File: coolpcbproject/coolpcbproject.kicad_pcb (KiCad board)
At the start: 2 copper layers, 106.7 x 38.1 mm, 24 parts, among them SW1 SW_Push, U1 ATmega32U4-A, Y1 16 MHz

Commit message: finished initial draft
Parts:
- added R5: 5.1K, Resistor_SMD:R_0805_2012Metric, B.Cu at (135.4, 89.0)
- added R6: 5.1K, Resistor_SMD:R_0805_2012Metric, B.Cu at (140.7, 89.0)
- added U2: USBLC6-2SC6, Package_TO_SOT_SMD:SOT-23-6, B.Cu at (137.9, 96.3)
- C1, C2, C3, C4, C5, C6, C7, D1, D2, D3, D4, F1, R1, R2, R3, R4, SW1, U1, Y1: moved to B.Cu
- USB1: value Molex-0548190589 -> HRO-TYPE-C-31-M-12; moved to B.Cu
- moved C1 44.0 mm to (169.7, 85.9), turned to -90 degrees
- moved C2 34.3 mm to (161.0, 85.9), turned to 90 degrees
- moved R4 32.2 mm to (173.6, 102.4), turned to -90 degrees
- moved R3 31.5 mm to (151.1, 101.9), turned to -90 degrees
- moved Y1 28.2 mm to (165.4, 85.9)
- moved R2 24.5 mm to (151.2, 98.2)
- moved F1 23.1 mm to (137.9, 91.8), turned to 180 degrees
- moved C3 19.7 mm to (156.0, 96.4), turned to -90 degrees
- moved SW1 17.6 mm to (140.8, 107.1)
- moved USB1 16.0 mm to (137.9, 77.8), turned to 0 degrees
- moved C5 13.9 mm to (173.6, 93.9), turned to -90 degrees
- moved C6 13.2 mm to (168.0, 105.4)
- moved C7 11.7 mm to (156.0, 101.3), turned to 90 degrees
- moved R1 11.6 mm to (151.4, 87.1), turned to -90 degrees
- moved U1 7.00 mm to (164.6, 97.0)
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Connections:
- C1 pad 1: (no net) -> GND
- C1 pad 2: (no net) -> Net-(C1-Pad2)
- C2 pad 1: (no net) -> GND
- C2 pad 2: (no net) -> Net-(C2-Pad2)
- C3 pad 1: (no net) -> Net-(C3-Pad1)
- C3 pad 2: (no net) -> GND
- C4 pad 1: (no net) -> GND
- C4 pad 2: (no net) -> +5V
- C5 pad 1: (no net) -> GND
- C5 pad 2: (no net) -> +5V
- C6 pad 1: (no net) -> GND
- C6 pad 2: (no net) -> +5V
- C7 pad 1: (no net) -> GND
- C7 pad 2: (no net) -> +5V
- D1 pad 1: (no net) -> row0
- D1 pad 2: (no net) -> Net-(D1-Pad2)
- D2 pad 1: (no net) -> row0
- D2 pad 2: (no net) -> Net-(D2-Pad2)
- D3 pad 1: (no net) -> row1
- D3 pad 2: (no net) -> Net-(D3-Pad2)
- D4 pad 1: (no net) -> row1
- D4 pad 2: (no net) -> Net-(D4-Pad2)
- F1 pad 1: (no net) -> Net-(F1-Pad1)
- F1 pad 2: (no net) -> +5V
- MX1 pad 1: (no net) -> col0
- MX1 pad 2: (no net) -> Net-(D1-Pad2)
- MX2 pad 1: (no net) -> col1
- MX2 pad 2: (no net) -> Net-(D2-Pad2)
- MX3 pad 1: (no net) -> col0
- MX3 pad 2: (no net) -> Net-(D3-Pad2)
- MX4 pad 1: (no net) -> col1
- MX4 pad 2: (no net) -> Net-(D4-Pad2)
- R1 pad 1: (no net) -> Net-(R1-Pad1)
- R1 pad 2: (no net) -> GND
- R2 pad 1: (no net) -> D+
- R2 pad 2: (no net) -> Net-(R2-Pad2)
- R3 pad 1: (no net) -> D-
- R3 pad 2: (no net) -> Net-(R3-Pad2)
- R4 pad 1: (no net) -> Net-(R4-Pad1)
- R4 pad 2: (no net) -> GND
- SW1 pad 1: (no net) -> GND
- SW1 pad 2: (no net) -> Net-(R1-Pad1)
- U1 pad 1: (no net) -> unconnected-(U1-Pad1)
- U1 pad 10: (no net) -> unconnected-(U1-Pad10)
- U1 pad 11: (no net) -> unconnected-(U1-Pad11)
- U1 pad 12: (no net) -> unconnected-(U1-Pad12)
- U1 pad 13: (no net) -> Net-(R1-Pad1)
- U1 pad 14: (no net) -> +5V
- U1 pad 15: (no net) -> GND
- U1 pad 16: (no net) -> Net-(C2-Pad2)
- U1 pad 17: (no net) -> Net-(C1-Pad2)
- U1 pad 18: (no net) -> unconnected-(U1-Pad18)
- U1 pad 19: (no net) -> unconnected-(U1-Pad19)
- U1 pad 2: (no net) -> +5V
- U1 pad 20: (no net) -> unconnected-(U1-Pad20)
- U1 pad 21: (no net) -> unconnected-(U1-Pad21)
- U1 pad 22: (no net) -> unconnected-(U1-Pad22)
- U1 pad 23: (no net) -> GND
- U1 pad 24: (no net) -> +5V
- U1 pad 25: (no net) -> unconnected-(U1-Pad25)
- U1 pad 26: (no net) -> unconnected-(U1-Pad26)
- U1 pad 27: (no net) -> row0
- U1 pad 28: (no net) -> col1
- U1 pad 29: (no net) -> col0
- U1 pad 3: (no net) -> Net-(R3-Pad2)
- U1 pad 30: (no net) -> row1
- U1 pad 31: (no net) -> unconnected-(U1-Pad31)
- U1 pad 32: (no net) -> unconnected-(U1-Pad32)
- U1 pad 33: (no net) -> Net-(R4-Pad1)
- U1 pad 34: (no net) -> +5V
- U1 pad 35: (no net) -> GND
- U1 pad 36: (no net) -> unconnected-(U1-Pad36)
- U1 pad 37: (no net) -> unconnected-(U1-Pad37)
- U1 pad 38: (no net) -> unconnected-(U1-Pad38)
- U1 pad 39: (no net) -> unconnected-(U1-Pad39)
- U1 pad 4: (no net) -> Net-(R2-Pad2)
- U1 pad 40: (no net) -> unconnected-(U1-Pad40)
- U1 pad 41: (no net) -> unconnected-(U1-Pad41)
- U1 pad 42: (no net) -> unconnected-(U1-Pad42)
- U1 pad 43: (no net) -> GND
- U1 pad 44: (no net) -> +5V
- U1 pad 5: (no net) -> GND
- U1 pad 6: (no net) -> Net-(C3-Pad1)
- U1 pad 7: (no net) -> +5V
- U1 pad 8: (no net) -> unconnected-(U1-Pad8)
- U1 pad 9: (no net) -> unconnected-(U1-Pad9)
- USB1 pad 1: (no net) -> GND
- USB1 pad 10: (no net) -> Net-(R6-Pad2)
- USB1 pad 11: (no net) -> Net-(F1-Pad1)
- USB1 pad 12: (no net) -> GND
- USB1 pad 13: (no net) -> GND
- USB1 pad 2: (no net) -> Net-(F1-Pad1)
- USB1 pad 3: (no net) -> unconnected-(USB1-Pad3)
- USB1 pad 4: (no net) -> Net-(R5-Pad2)
- USB1 pad 5: (no net) -> D- IN
- USB1 pad 6: (no net) -> D+ IN
- USB1 pad 7: (no net) -> D- IN
- USB1 pad 8: (no net) -> D+ IN
- USB1 pad 9: (no net) -> unconnected-(USB1-Pad9)
- Y1 pad 1: (no net) -> Net-(C2-Pad2)
- Y1 pad 2: (no net) -> GND
- Y1 pad 3: (no net) -> Net-(C1-Pad2)
- Y1 pad 4: (no net) -> GND
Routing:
- net GND: track 0.00 -> 138.4 mm
- net +5V: track 0.00 -> 75.8 mm, vias 0 -> 2
- net row1: track 0.00 -> 58.8 mm
- net col1: track 0.00 -> 56.5 mm
- net row0: track 0.00 -> 48.5 mm
- net col0: track 0.00 -> 37.2 mm
- net Net-(R1-Pad1): track 0.00 -> 36.3 mm, vias 0 -> 2
- net Net-(R3-Pad2): track 0.00 -> 17.2 mm
- net D- IN: track 0.00 -> 13.5 mm
- net Net-(R2-Pad2): track 0.00 -> 13.0 mm
- net D+ IN: track 0.00 -> 11.8 mm
- net Net-(C2-Pad2): track 0.00 -> 11.0 mm
- net Net-(D1-Pad2): track 0.00 -> 8.54 mm
- net Net-(C1-Pad2): track 0.00 -> 8.52 mm
- net Net-(D4-Pad2): track 0.00 -> 8.50 mm
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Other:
- board size 106.7 x 38.1 mm -> 90.9 x 38.1 mm

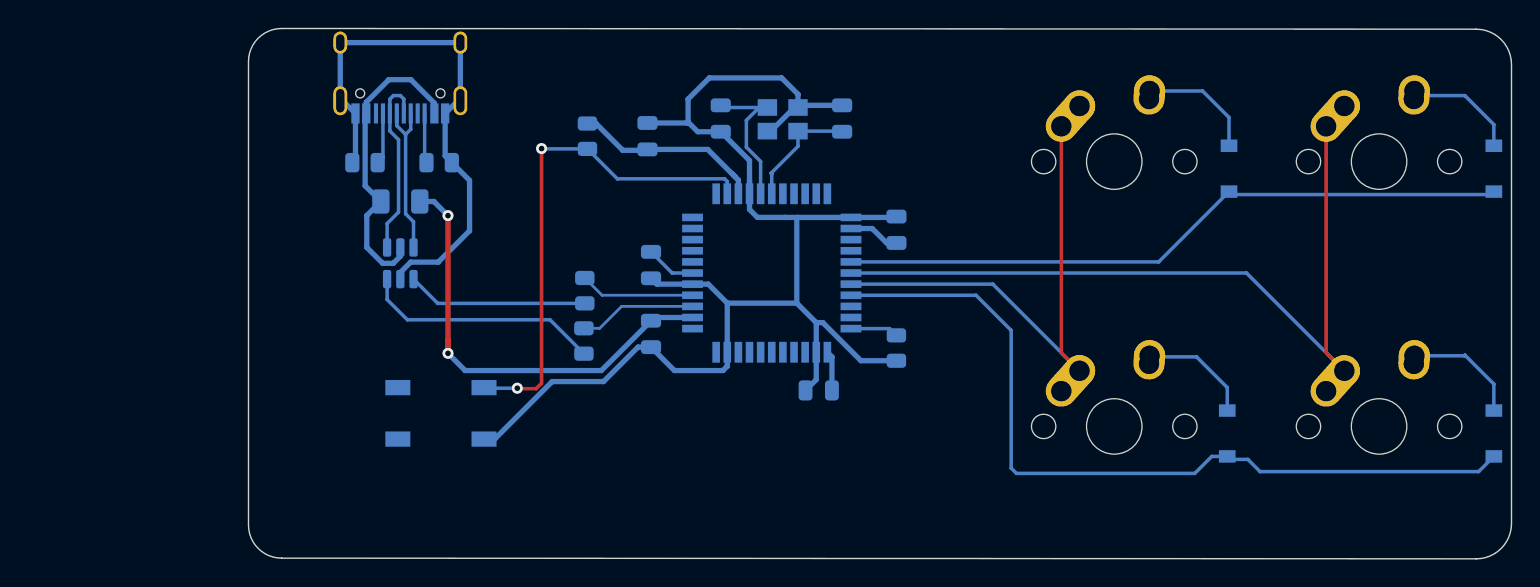
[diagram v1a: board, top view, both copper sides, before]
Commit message: initial draft 2
all routing complete, all DRC bugs removed
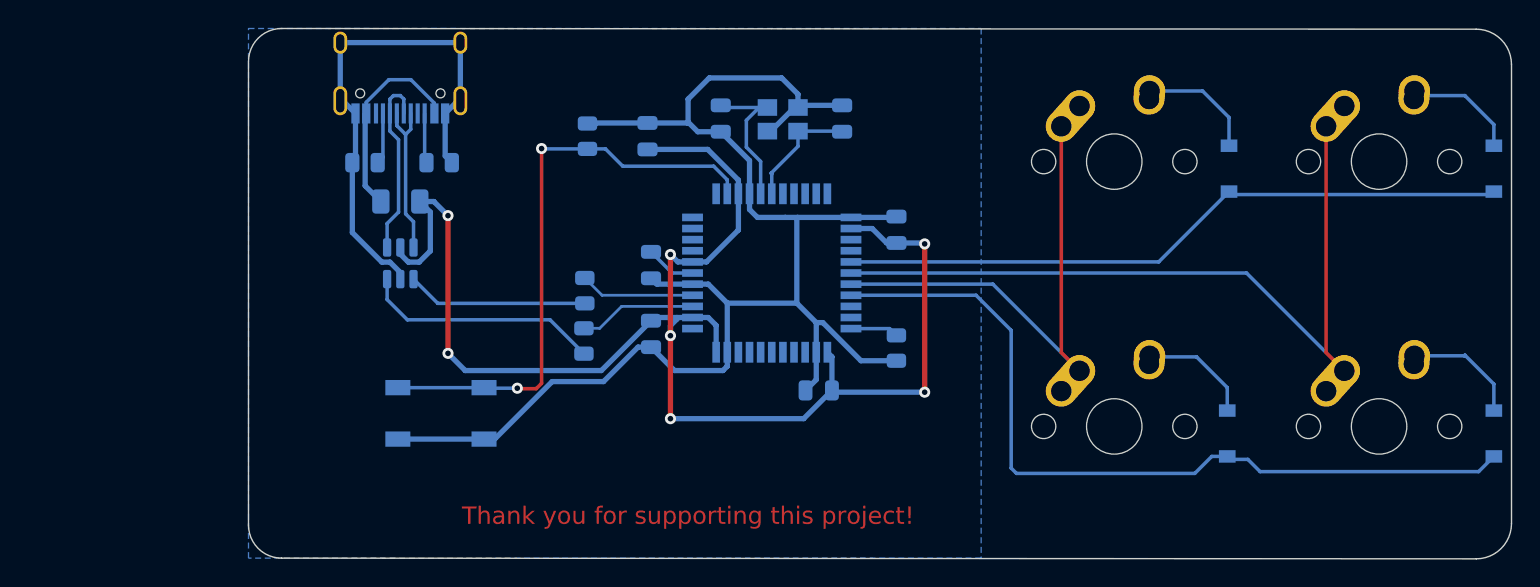
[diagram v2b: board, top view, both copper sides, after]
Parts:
- added G***: LOGO, logolibrary:veglogo, F.Cu at (132.0, 108.5)
- turned R1 to 90 degrees
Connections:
- F1 pad 1: Net-(F1-Pad1) -> +5V
- F1 pad 2: +5V -> Vcc
- R2 pad 2: Net-(R2-Pad2) -> D+ OUT
- R3 pad 2: Net-(R3-Pad2) -> D- OUT
- U1 pad 3: Net-(R3-Pad2) -> D-
- U1 pad 4: Net-(R2-Pad2) -> D+
- USB1 pad 11: Net-(F1-Pad1) -> Vcc
- USB1 pad 2: Net-(F1-Pad1) -> Vcc
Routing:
- net +5V: track 75.8 -> 111.9 mm, vias 2 -> 7
- net Net-(R3-Pad2): track 17.2 -> 0.00 mm
- net D- OUT: track 0.00 -> 17.2 mm
- net Vcc: track 0.00 -> 14.7 mm
- net Net-(R2-Pad2): track 13.0 -> 0.00 mm
- net D+ OUT: track 0.00 -> 13.0 mm
- net GND: track 138.4 -> 146.6 mm
- net Net-(R1-Pad1): track 36.3 -> 42.6 mm
- net Net-(C2-Pad2): track 11.0 -> 10.4 mm
- added copper zone on B.Cu, net GND
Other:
- board text added: "Thank you for supporting this project!"

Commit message: aesthetic changes
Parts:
- removed the G*** at (132.0, 108.5)
- added G***: LOGO, veglogo, F.Cu at (134.5, 101.2)
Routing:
- net +5V: track 111.9 -> 110.9 mm
